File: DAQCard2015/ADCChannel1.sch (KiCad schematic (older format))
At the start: 16 parts, among them U2 THS4524IDBTR, U3 AD9219

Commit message: propogate previous changes to other channels and schematic
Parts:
- removed R4, R5: Rt, Resistors_SMD:R_0603, symbol R
- removed U2: THS4524IDBTR, Housings_SSOP:TSSOP-38_4.4x9.7mm_Pitch0.5mm, symbol THS4524IDBTR
- removed U3: AD9219, SMD_Packages:QFN-48-1EP, symbol AD9219
- added R8, R9: Rt, Resistors_SMD:R_0603, symbol R
- added U3: THS4524IDBTR, Housings_SSOP:TSSOP-38_4.4x9.7mm_Pitch0.5mm, symbol THS4524IDBTR
- added U4: AD9219, extras:QFN-48-1EP, symbol AD9219
- C8: footprint (none) -> Capacitors_SMD:C_0805
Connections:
- net 1V8ana: now also U4.1 (AVDD), U4.10 (AVDD), U4.2 (AVDD), U4.27 (AVDD), U4.32 (AVDD), U4.35 (AVDD), U4.36 (AVDD), U4.39 (AVDD), U4.41 (SENSE), U4.45 (AVDD), U4.46 (AVDD), U4.5 (AVDD), U4.6 (AVDD), U4.9 (AVDD)
- net 1V8dig: now also U4.12 (DRVDD), U4.25 (DRVDD)
- net 3V3ana: now also U3.20 (VS4+), U3.25 (VS3+), U3.30 (VS2+), U3.35 (VS1+)
- net ADC_CSB: now also U4.30 (CSB)
- net ADC_SCLK: now also U4.28 (SCLK/DTP)
- net ADC_SDIO: now also U4.29 (SDIO/ODM)
- net ADC_Vref: now also U4.42 (VREF)
- net CHA+: now also U3.36 (VOUT1+), U4.33 (VIN+A)
- net CHA-: now also U3.37 (VOUT1-), U4.34 (VIN-A)
- net CHB+: now also U3.31 (VOUT2+), U4.38 (VIN+B)
- net CHB-: now also U3.32 (VOUT2-), U4.37 (VIN-B)
- net CHC+: now also U3.26 (VOUT3+), U4.47 (VIN+C)
- net CHC-: now also U3.27 (VOUT3-), U4.48 (VIN-C)
- net CHD+: now also U3.21 (VOUT4+), U4.4 (VIN+D)
- net CHD-: now also U3.22 (VOUT4-), U4.3 (VIN-D)
- net D+A: now also U4.20 (D+A)
- net D+B: now also U4.18 (D+B)
- net D+C: now also U4.16 (D+C)
- net D+D: now also U4.14 (D+D)
- net D-A: now also U4.19 (D-A)
- net D-B: now also U4.17 (D-B)
- net D-C: now also U4.15 (D-C)
- net D-D: now also U4.13 (D-D)
- net DCO+: now also U4.24 (DCO+)
- net DCO-: now also U4.23 (DCO-)
- net EXT_CHA+: now also R6.1
- net EXT_CHA-: now also R6.2
- net EXT_CHB+: now also R7.1
- net EXT_CHB-: now also R7.2
- net EXT_CHC+: now also R8.1; no longer R6.1
- net EXT_CHC-: now also R8.2; no longer R6.2
- net EXT_CHD+: now also R9.1; no longer R7.1
- net EXT_CHD-: now also R9.2; no longer R7.2
- net FCO+: now also U4.22 (FCO+)
- net FCO-: now also U4.21 (FCO-)
- net GND: now also U3.10 (VS-), U3.15 (VS-), U3.23 (VS-), U3.24 (VS-), U3.28 (VS-), U3.29 (VS-), U3.33 (VS-), U3.34 (VS-), U3.38 (VS-), U3.5 (VS-), U4.0 (AGND), U4.11 (DRGND), U4.26 (DRGND), U4.31 (PDWN)
- net Vocm: now also U3.14 (VOCM3), U3.19 (VOCM4), U3.4 (VOCM1), U3.9 (VOCM2)
- net at C6.1: now also U4.8 (CLK+)
- net at RP1.16 (R1), RP3.1 (P1): now also U3.2 (Vin1+)
- net at RP1.15 (R2), RP3.2 (P2): now also U3.3 (VIN1-)
- net at RP1.14 (R3), RP3.3 (P3): now also U3.7 (VIN2+)
- net at RP1.13 (R4), RP3.4 (P4): now also U3.8 (VIN2-)
- net at R10.2: now also U4.40 (RBIAS)
- net at C10.2, C8.2, C9.1: now also U4.43 (REFB)
- net at C7.1, C8.1, C9.2: now also U4.44 (REFT)
- net at C5.1: now also U4.7 (CLK-)
- net at RP1.12 (R5), RP2.1 (P1): now also U3.12 (VIN3+)
- net at RP1.11 (R6), RP2.2 (P2): now also U3.13 (VIN3-)
- net at RP1.10 (R7), RP2.3 (P3): now also U3.17 (VIN4+)
- net at RP1.9 (R8), RP2.4 (P4): now also U3.18 (VIN4-)
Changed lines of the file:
@@
 $EndDescr
 $Comp
-L AD9219 U3
-U 1 1 55CB5758
+L AD9219 U4
+U 1 1 55EBCB03
 P 9050 3700
-F 0 "U3" H 8250 4650 60  0000 C CNN
+F 0 "U4" H 8250 4650 60  0000 C CNN
 F 1 "AD9219" H 9050 3800 60  0000 C CNN
-F 2 "SMD_Packages:QFN-48-1EP" H 8650 3700 60  0001 C CNN
+F 2 "extras:QFN-48-1EP" H 8650 3700 60  0001 C CNN
 F 3 "" H 8650 3700 60  0000 C CNN
 	1    9050 3700
@@
 $Comp
 L C C5
-U 1 1 55CB5765
+U 1 1 55EBCB0F
 P 7550 3650
 F 0 "C5" H 7575 3750 50  0000 L CNN
@@
 $Comp
 L C C6
-U 1 1 55CB5746
+U 1 1 55EBCAF6
 P 7550 3950
 F 0 "C6" H 7575 4050 50  0000 L CNN
@@
 $Comp
 L C C10
-U 1 1 55CB578F
+U 1 1 55EBCB27
 P 9300 1750
 F 0 "C10" H 9325 1850 50  0000 L CNN
@@
 $Comp
 L C C7
-U 1 1 55CB5768
+U 1 1 55EBCB17
 P 8600 1750
 F 0 "C7" H 8625 1850 50  0000 L CNN
@@
 $Comp
 L C C9
-U 1 1 55CB576F
+U 1 1 55EBCB1E
 P 8950 1650
 F 0 "C9" H 8975 1750 50  0000 L CNN
@@
 $Comp
 L R R10
-U 1 1 55CB5780
+U 1 1 55EBCB1F
 P 9900 1950
 F 0 "R10" V 9980 1950 50  0000 C CNN
@@
 LVDS Output Signals
 $Comp
-L THS4524IDBTR U2
-U 1 1 55CB579D
+L THS4524IDBTR U3
+U 1 1 55EBCB30
 P 4400 3700
-F 0 "U2" H 4700 2750 60  0000 C CNN
+F 0 "U3" H 4700 2750 60  0000 C CNN
 F 1 "THS4524IDBTR" H 4400 4850 60  0000 C CNN
 F 2 "Housings_SSOP:TSSOP-38_4.4x9.7mm_Pitch0.5mm" H 4600 3800 60  0001 C CNN
@@
 EXT_CHD-
 $Comp
-L R R7
-U 1 1 55CB57A8
+L R R9
+U 1 1 55EBCB36
 P 1850 4350
-F 0 "R7" V 1930 4350 50  0000 C CNN
+F 0 "R9" V 1930 4350 50  0000 C CNN
 F 1 "Rt" V 1850 4350 50  0000 C CNN
 F 2 "Resistors_SMD:R_0603" V 1780 4350 30  0001 C CNN
@@
 $EndComp
 $Comp
-L R R6
-U 1 1 55CB57B1
+L R R8
+U 1 1 55EBCB40
 P 1850 3850
-F 0 "R6" V 1930 3850 50  0000 C CNN
+F 0 "R8" V 1930 3850 50  0000 C CNN
 F 1 "Rt" V 1850 3850 50  0000 C CNN
 F 2 "Resistors_SMD:R_0603" V 1780 3850 30  0001 C CNN
@@
 $EndComp
 $Comp
-L R R5
-U 1 1 55CB57B5
+L R R7
+U 1 1 55EBCB46
 P 1850 3350
-F 0 "R5" V 1930 3350 50  0000 C CNN
+F 0 "R7" V 1930 3350 50  0000 C CNN
 F 1 "Rt" V 1850 3350 50  0000 C CNN
 F 2 "Resistors_SMD:R_0603" V 1780 3350 30  0001 C CNN
@@
 $EndComp
 $Comp
-L R R4
-U 1 1 55CB57BD
+L R R6
+U 1 1 55EBCB4A
 P 1850 2850
-F 0 "R4" V 1930 2850 50  0000 C CNN
+F 0 "R6" V 1930 2850 50  0000 C CNN
 F 1 "Rt" V 1850 2850 50  0000 C CNN
 F 2 "Resistors_SMD:R_0603" V 1780 2850 30  0001 C CNN
@@
 $Comp
 L R_PACK4 RP2
-U 1 1 55CB57C4
+U 1 1 55EBCB54
 P 4250 5150
 F 0 "RP2" H 4250 5600 50  0000 C CNN
@@
 $Comp
 L R_PACK4 RP3
-U 1 1 55CB574C
+U 1 1 55EBCAFD
 P 4300 2450
 F 0 "RP3" H 4300 2900 50  0000 C CNN
@@
 $Comp
 L R_PACK8 RP1
-U 1 1 55CB57CA
+U 1 1 55EBCB5D
 P 2750 3600
 F 0 "RP1" H 2750 4050 50  0000 C CNN
@@
 $Comp
 L C C8
-U 1 1 55EB3809
+U 1 1 55EBCB64
 P 8950 1450
 F 0 "C8" H 8975 1550 50  0000 L CNN
 F 1 "2.2uF" H 8975 1350 50  0000 L CNN
-F 2 "" H 8988 1300 30  0000 C CNN
+F 2 "Capacitors_SMD:C_0805" H 8988 1300 30  0001 C CNN
 F 3 "" H 8950 1450 60  0000 C CNN
 	1    8950 1450

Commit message: Various updates to DAQ board focusing on power system
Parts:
- U3: footprint Housings_SSOP:TSSOP-38_4.4x9.7mm_Pitch0.5mm -> extras:TSSOP-38_4.4x9.7mm_Pitch0.5mm
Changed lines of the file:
@@
 F 0 "U3" H 4700 2750 60  0000 C CNN
 F 1 "THS4524IDBTR" H 4400 4850 60  0000 C CNN
-F 2 "Housings_SSOP:TSSOP-38_4.4x9.7mm_Pitch0.5mm" H 4600 3800 60  0001 C CNN
+F 2 "extras:TSSOP-38_4.4x9.7mm_Pitch0.5mm" H 4600 3800 60  0001 C CNN
 F 3 "" H 4600 3800 60  0000 C CNN
 	1    4400 3700

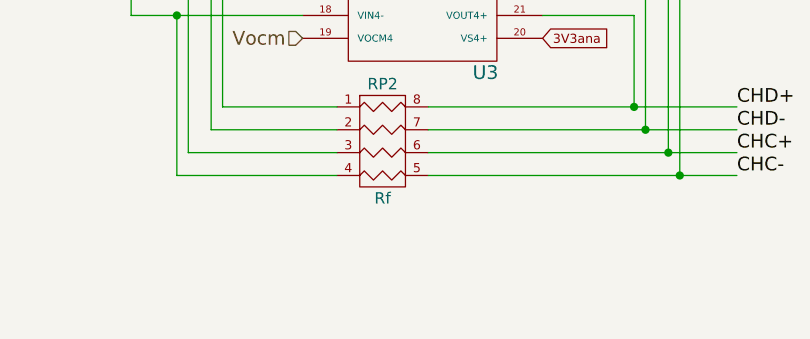
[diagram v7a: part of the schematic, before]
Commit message: Update to DAQ Board including adding an JTAG header and hooking up external clock and trigger
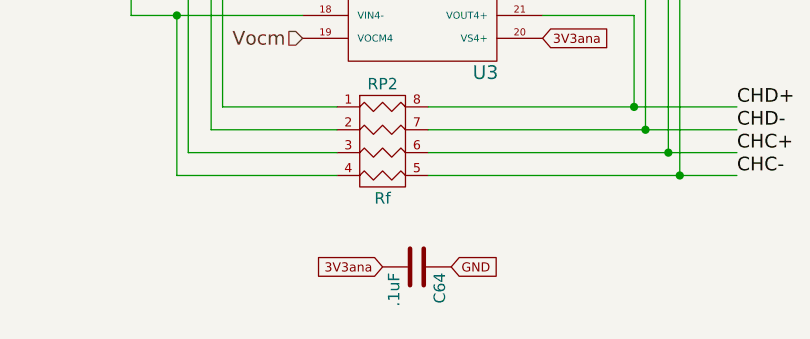
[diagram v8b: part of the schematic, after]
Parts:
- added C64: .1uF, Capacitors_SMD:C_0603, symbol C
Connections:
- net 3V3ana: now also C64.2
- net GND: now also C64.1
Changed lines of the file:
@@
 Text GLabel 8100 4150 0    40   Input ~ 0
 GND
+$Comp
+L C C64
+U 1 1 5606444B
+P 4400 5500
+F 0 "C64" H 4425 5600 50  0000 L CNN
+F 1 ".1uF" H 4425 5400 50  0000 L CNN
+F 2 "Capacitors_SMD:C_0603" H 4438 5350 30  0001 C CNN
+F 3 "" H 4400 5500 60  0000 C CNN
+	1    4400 5500
+	0    1    1    0
+$EndComp
+Text GLabel 4250 5500 0    40   Input ~ 0
+3V3ana
+Text GLabel 4550 5500 2    40   Input ~ 0
+GND
 $EndSCHEMATC
